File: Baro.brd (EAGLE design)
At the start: 15.2 x 12.7 mm, 9 parts

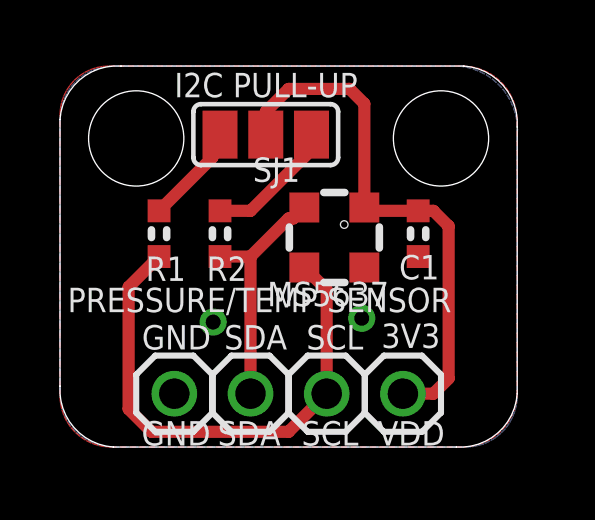
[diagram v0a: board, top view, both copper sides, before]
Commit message: Volt. regulator and FETs added.
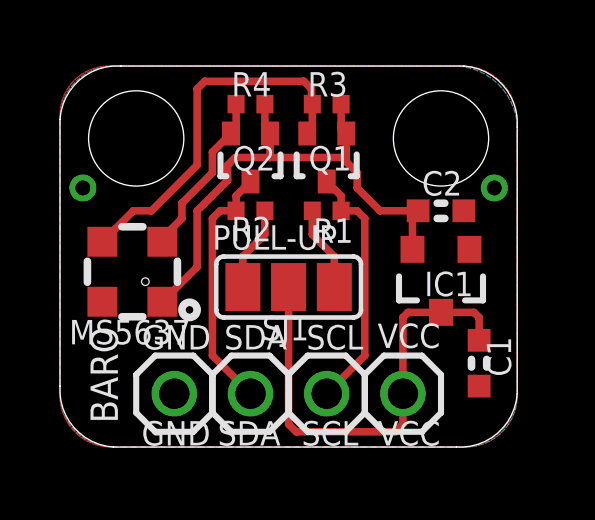
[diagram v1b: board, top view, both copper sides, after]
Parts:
- added C2: 1uF, freetronics-master-v1:0603
- added IC1: MCP1700T-3302E/TT, freetronics-master-v1:SOT23-3
- added Q1, Q2: RJU003N03 N-MOSFET, freetronics-jon:SOT32-3
- added R3, R4: 10K 0402, freetronics-jon:0402
- C1: value 100nF -> 1uF; device freetronics-master-v1.1:0603 -> freetronics-master-v1:0603
- R1, R2: value 10K -> 10K 0402; device freetronics-master-v1.1:0603 -> freetronics-jon:0402
- moved MS5637 6.83 mm to (2.41, 5.84), turned to 180 degrees
- moved R1 5.64 mm to (8.89, 7.87), turned to 180 degrees
- moved SJ1 5.14 mm to (7.62, 5.33), turned to 0 degrees
- moved C1 4.77 mm to (14.0, 2.79)
- moved R2 1.27 mm to (6.35, 7.87), turned to 0 degrees
- renumbered VDD to VCC
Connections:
- removed net N$2: C1.1, MS5637.1, SJ1.2, VCC.1
- new net 3.3V: C2.1, IC1.2, MS5637.1, Q1.1, Q2.1, R3.2, R4.2
- new net N$3: C1.1, IC1.3, SJ1.2, VCC.1
- new net SCL: Q1.3, R1.1, SCL.1
- new net SDA: Q2.3, R2.1, SDA.1
- net GND: now also C2.2, IC1.1
- net N$1: now also Q1.2, R3.1; no longer R1.1, SCL.1
- net N$4: now also Q2.2, R4.1; no longer R2.1, SDA.1
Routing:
- net 3.3V: track 0.00 -> 18.2 mm
- net N$2: track 17.9 -> 0.00 mm
- net N$3: track 0.00 -> 15.8 mm
- net SDA: track 0.00 -> 8.44 mm
- net SCL: track 0.00 -> 8.44 mm
- net N$1: track 17.5 -> 12.5 mm
- net N$4: track 8.06 -> 5.71 mm
- net N$6: track 4.61 -> 3.20 mm
- net N$5: track 3.38 -> 2.84 mm
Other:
- board text added: "2.3-6V"
- board text added: "BARO"
- board text added: "PULL-UP"
- board text added: "VCC"
- board text added: "v1.0"
- board text removed: "3V3"
- board text removed: "I2C PULL-UP"

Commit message: Noted Adelmo Eloy as the designer Added license info to schematic Relocated decoupling cap to near sensor Improved ground connection to regulator Added notes to schematic about operating ranges Changed I2C pull-ups to 4K7
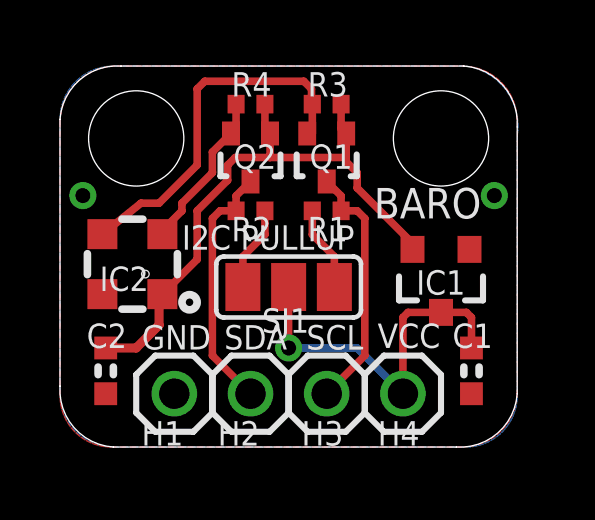
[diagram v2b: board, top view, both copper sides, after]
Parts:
- removed MS5637: MS563702BA03, freetronics-original:MS5637
- added IC2: MS563702BA03, freetronics-original:MS5637
- H1: value M01PTH -> GND
- H2: value M01PTH -> SDA
- H3: value M01PTH -> SCL
- H4: value M01PTH -> VCC
- R1, R2: value 10K 0402 -> 4K7 0402
- moved C2 12.4 mm to (1.52, 2.54), turned to 270 degrees
- moved C1 0.36 mm to (13.7, 2.54)
- renumbered GND to H1, SCL to H3, SDA to H2, VCC to H4
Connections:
- net 3.3V: now also IC2.1; no longer MS5637.1
- net GND: now also IC2.4; no longer MS5637.4
- net N$1: now also IC2.3; no longer MS5637.3
- net N$4: now also IC2.2; no longer MS5637.2
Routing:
- net N$3: track 15.8 -> 12.6 mm, vias 0 -> 1
- net 3.3V: track 18.2 -> 20.2 mm
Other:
- board text added: "(c) 2014 Freetronics"
- board text added: "I2C PULLUP"
- board text removed: "(c) 2013 Freetronics"
- board text removed: "PULL-UP"

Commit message: Bridged I2C pullup jumpers Shortened URL
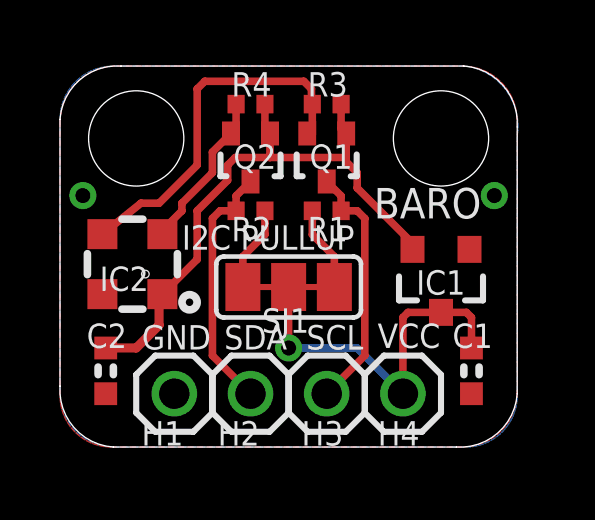
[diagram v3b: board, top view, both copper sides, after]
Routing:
- net N$2: track 0.00 -> 0.51 mm
- net N$7: track 0.00 -> 0.51 mm
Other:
- board text added: "tron.cc/baro"
- board text added: "v1.1"
- board text removed: "v1.0"
- board text removed: "www.freetronics.com/baro"
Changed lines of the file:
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@@
 <?xml version="1.0" encoding="utf-8"?>
 <!DOCTYPE eagle SYSTEM "eagle.dtd">
-<eagle version="6.3">
+<eagle version="6.5.0">
 <drawing>
 <settings>
@@
 <wire x1="11.684" y1="6.604" x2="12.7" y2="7.62" width="0.254" layer="22" curve="90.022562"/>
 <wire x1="12.7" y1="7.62" x2="11.811" y2="8.636" width="0.254" layer="22" curve="89.988722"/>
-<text x="14.859" y="4.318" size="0.7366" layer="22" font="vector" ratio="16" rot="MR0">www.freetronics.com/baro</text>
+<text x="12.319" y="4.318" size="0.9144" layer="22" font="vector" ratio="16" rot="MR0">tron.cc/baro</text>
 <text x="10.922" y="9.144" size="0.8636" layer="22" font="vector" ratio="18" rot="MR0">SKU: BARO</text>
 <text x="12.065" y="7.239" size="1.016" layer="22" font="vector" ratio="15" rot="MR0">freetronics</text>
@@
 <text x="10.4648" y="7.62" size="1.016" layer="21" font="vector" ratio="15">BARO</text>
 <circle x="4.318" y="4.826" radius="0.254" width="0.254" layer="21"/>
-<text x="2.032" y="3.81" size="1.016" layer="22" ratio="15" rot="MR270">v1.0</text>
+<text x="2.032" y="3.81" size="1.016" layer="22" ratio="15" rot="MR270">v1.1</text>
 <circle x="4.318" y="5.08" radius="0.254" width="0.254" layer="51"/>
 </plain>
@@
 <wire x1="6.096" y1="6.35" x2="6.096" y2="5.334" width="0.254" layer="1"/>
 </signal>
+<signal name="N$2">
+<wire x1="6.604" y1="5.334" x2="7.112" y2="5.334" width="0.2032" layer="1"/>
+</signal>
+<signal name="N$7">
+<wire x1="8.128" y1="5.334" x2="8.636" y2="5.334" width="0.2032" layer="1"/>
+</signal>
 </signals>
+<errors>
+</errors>
 </board>
 </drawing>
